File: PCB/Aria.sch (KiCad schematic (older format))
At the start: 0 parts

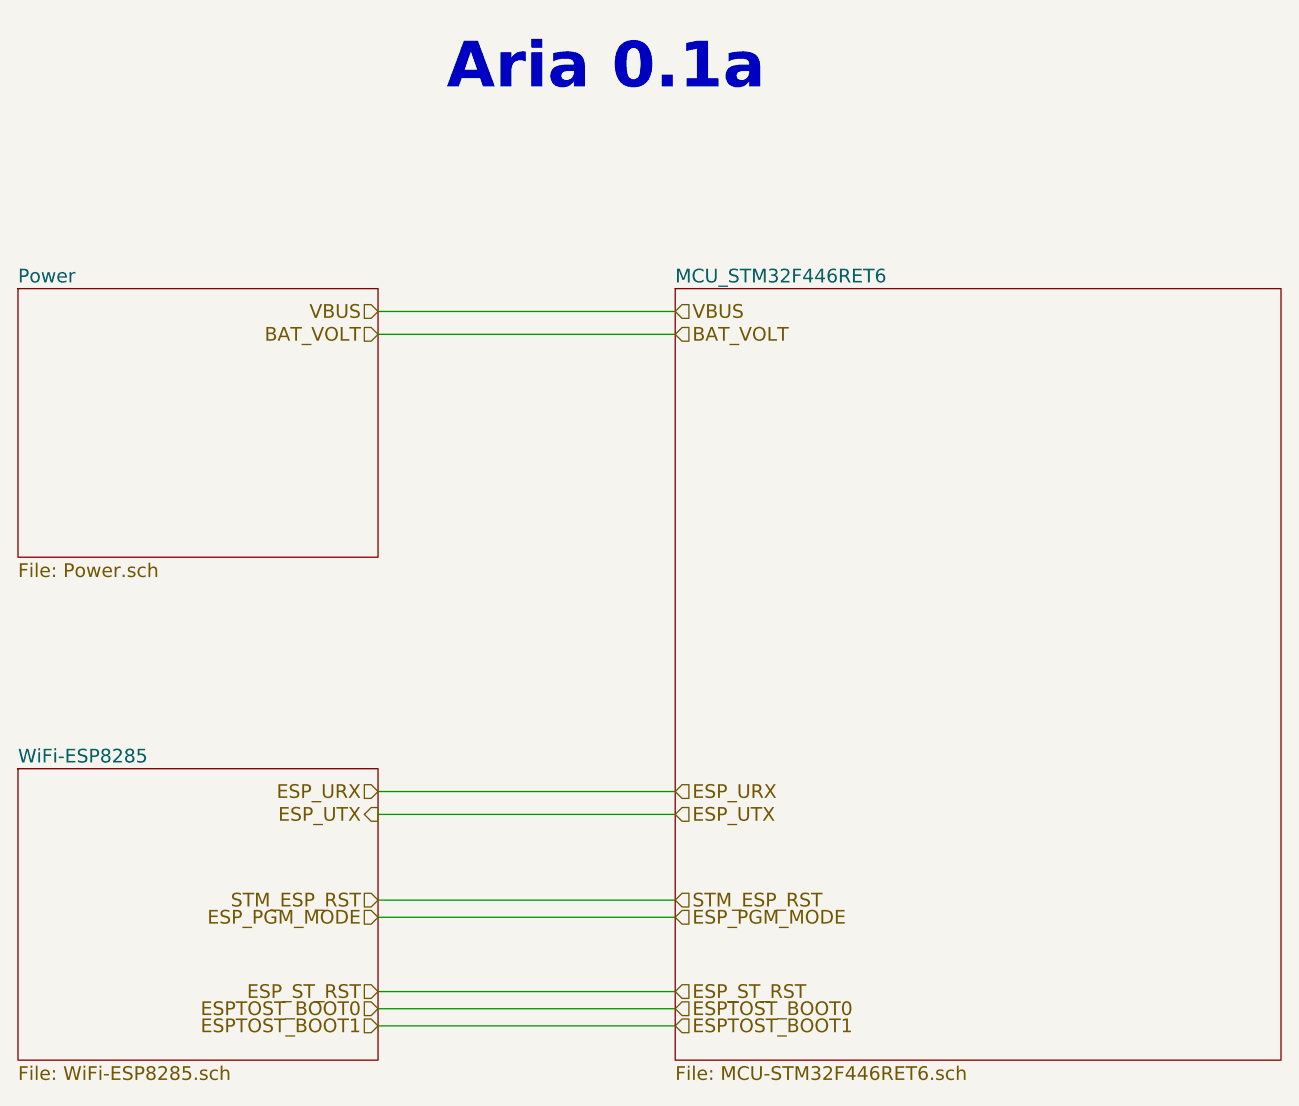
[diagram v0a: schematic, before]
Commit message: Finished Placement and Mapping
Components placed, some routing completed. pin header mapping figured
out.
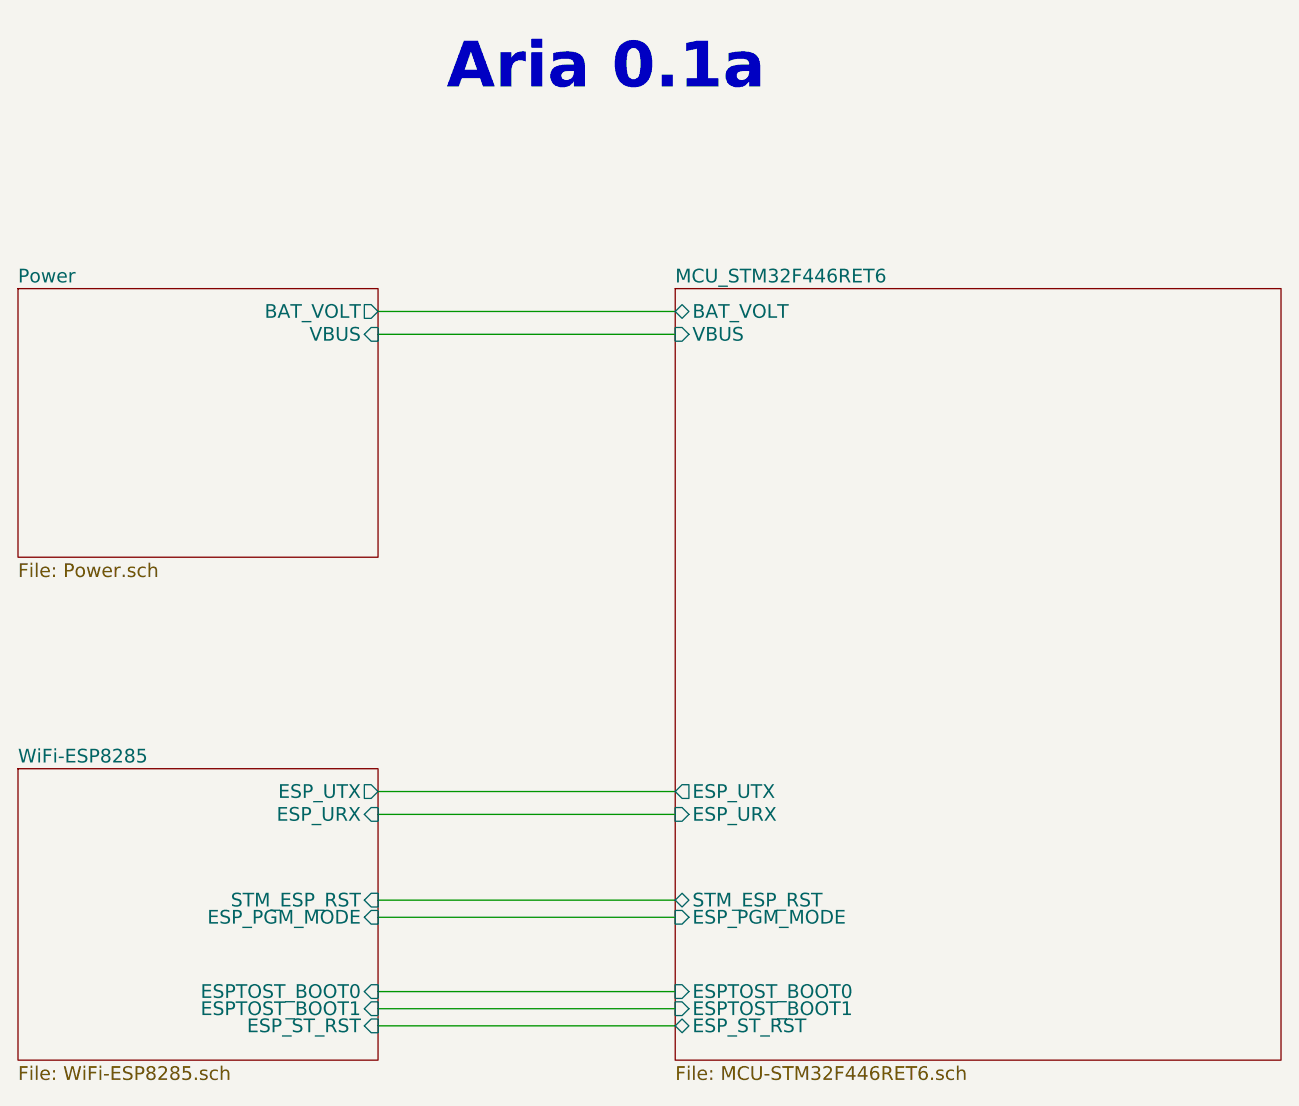
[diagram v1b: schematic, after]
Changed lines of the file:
@@
 F0 "Power" 60
 F1 "Power.sch" 60
-$EndSheet
-$Sheet
-S 6125 2000 2650 3375
-U 57E9EA74
-F0 "MCU_STM32F446RET6" 60
-F1 "MCU-STM32F446RET6.sch" 60
+F2 "VBUS" I R 4825 2200 60
+F3 "BAT_VOLT" O R 4825 2100 60
 $EndSheet
 $Sheet
@@
 F0 "WiFi-ESP8285" 60
 F1 "WiFi-ESP8285.sch" 60
+F2 "ESP_URX" I R 4825 4300 60
+F3 "ESP_UTX" O R 4825 4200 60
+F4 "STM_ESP_RST" I R 4825 4675 60
+F5 "ESP_PGM_MODE" I R 4825 4750 60
+F6 "ESP_ST_RST" I R 4825 5225 60
+F7 "ESPTOST_BOOT0" I R 4825 5075 60
+F8 "ESPTOST_BOOT1" I R 4825 5150 60
 $EndSheet
-Text HLabel 4825 2100 0    60   Input ~ 0
-VBUS
-Text HLabel 4825 2200 0    60   Input ~ 0
-BAT_VOLT
-Text HLabel 4825 4200 0    60   Input ~ 0
-ESP_URX
-Text HLabel 4825 4300 0    60   Output ~ 0
-ESP_UTX
-Text HLabel 4825 4675 0    60   Input ~ 0
-STM_ESP_RST
-Text HLabel 4825 4750 0    60   Input ~ 0
-ESP_PGM_MODE
-Text HLabel 4825 5075 0    60   Input ~ 0
-ESP_ST_RST
-Text HLabel 4825 5150 0    60   Input ~ 0
-ESPTOST_BOOT0
-Text HLabel 4825 5225 0    60   Input ~ 0
-ESPTOST_BOOT1
-Text HLabel 6125 4200 2    60   Input ~ 0
-ESP_URX
-Text HLabel 6125 4300 2    60   Input ~ 0
-ESP_UTX
-Text HLabel 6125 4675 2    60   Input ~ 0
-STM_ESP_RST
-Text HLabel 6125 4750 2    60   Input ~ 0
-ESP_PGM_MODE
-Text HLabel 6125 5075 2    60   Input ~ 0
-ESP_ST_RST
-Text HLabel 6125 5150 2    60   Input ~ 0
-ESPTOST_BOOT0
-Text HLabel 6125 5225 2    60   Input ~ 0
-ESPTOST_BOOT1
-Text HLabel 6125 2100 2    60   Input ~ 0
-VBUS
-Text HLabel 6125 2200 2    60   Input ~ 0
-BAT_VOLT
 Wire Wire Line
 	4825 4200 6125 4200
@@
 Text Notes 5125 1150 0    200  ~ 40
 Aria 0.1a
+$Sheet
+S 6125 2000 2650 3375
+U 57E9EA74
+F0 "MCU_STM32F446RET6" 60
+F1 "MCU-STM32F446RET6.sch" 60
+F2 "ESP_ST_RST" B L 6125 5225 60
+F3 "STM_ESP_RST" B L 6125 4675 60
+F4 "ESP_UTX" O L 6125 4200 60
+F5 "ESP_URX" I L 6125 4300 60
+F6 "ESP_PGM_MODE" I L 6125 4750 60
+F7 "VBUS" I L 6125 2200 60
+F8 "ESPTOST_BOOT0" I L 6125 5075 60
+F9 "ESPTOST_BOOT1" I L 6125 5150 60
+F10 "BAT_VOLT" B L 6125 2100 60
+$EndSheet
 $EndSCHEMATC
